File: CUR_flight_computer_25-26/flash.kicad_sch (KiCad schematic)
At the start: 16 parts, among them J1 Micro_SD_Card_Det1, U10 W25Q32JVSS

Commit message: Apply ESDA5V3SC5 MPNs
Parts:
- D11, D12: MPN ESDA6V1SC5 -> ESDA5V3SC5
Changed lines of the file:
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@@
 			)
 		)
-		(property "MPN" "ESDA6V1SC5"
+		(property "MPN" "ESDA5V3SC5"
 			(at 78.74 168.91 0)
 			(effects
@@
 			)
 		)
-		(property "MPN" "ESDA6V1SC5"
+		(property "MPN" "ESDA5V3SC5"
 			(at 107.95 168.91 0)
 			(effects

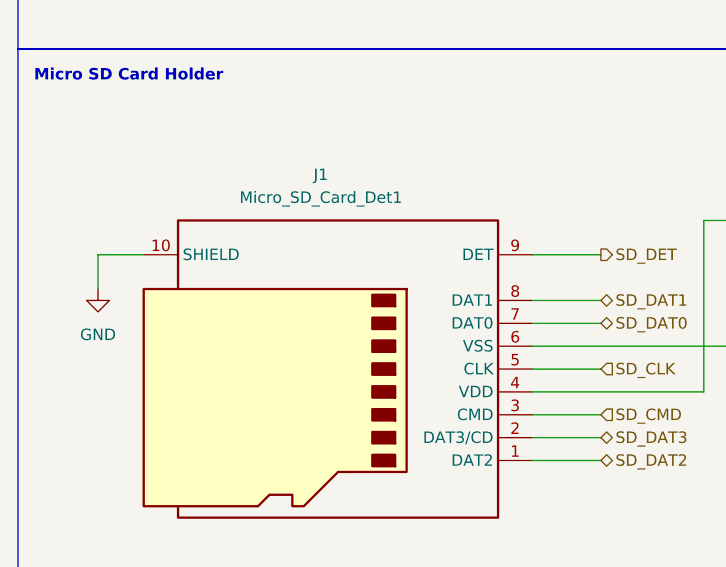
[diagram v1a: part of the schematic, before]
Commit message: BOM optimize 4.7u to 10u caps
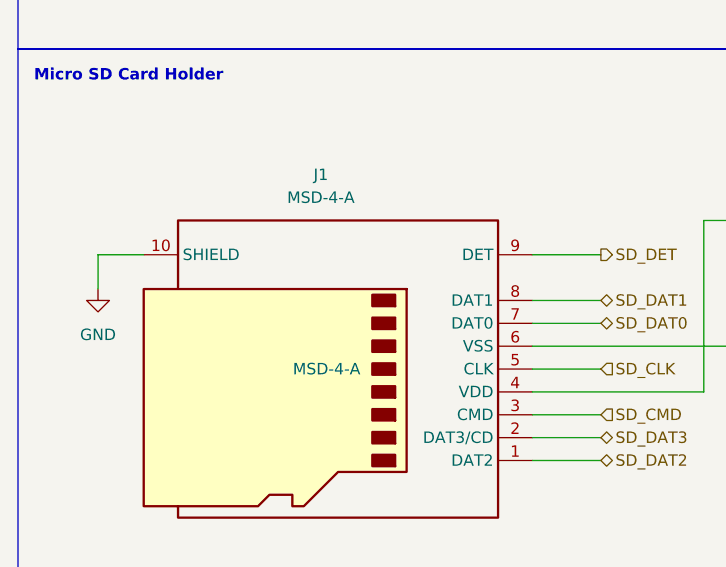
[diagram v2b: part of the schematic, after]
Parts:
- C32: MPN GRM188R61A106ME69D -> LMK107BBJ106MALT
- J1: value Micro_SD_Card_Det1 -> MSD-4-A; MPN (none) -> MSD-4-A
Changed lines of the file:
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@@
 			)
 		)
-		(property "MPN" "GRM188R61A106ME69D"
+		(property "MPN" "LMK107BBJ106MALT"
 			(at 106.68 111.76 0)
 			(effects
@@
 			)
 		)
-		(property "Value" "Micro_SD_Card_Det1"
+		(property "Value" "MSD-4-A"
 			(at 47.625 105.41 0)
 			(effects
@@
 			)
 		)
+		(property "MPN" "MSD-4-A"
+			(at 48.26 124.46 0)
+			(effects
+				(font
+					(size 1.27 1.27)
+				)
+			)
+		)

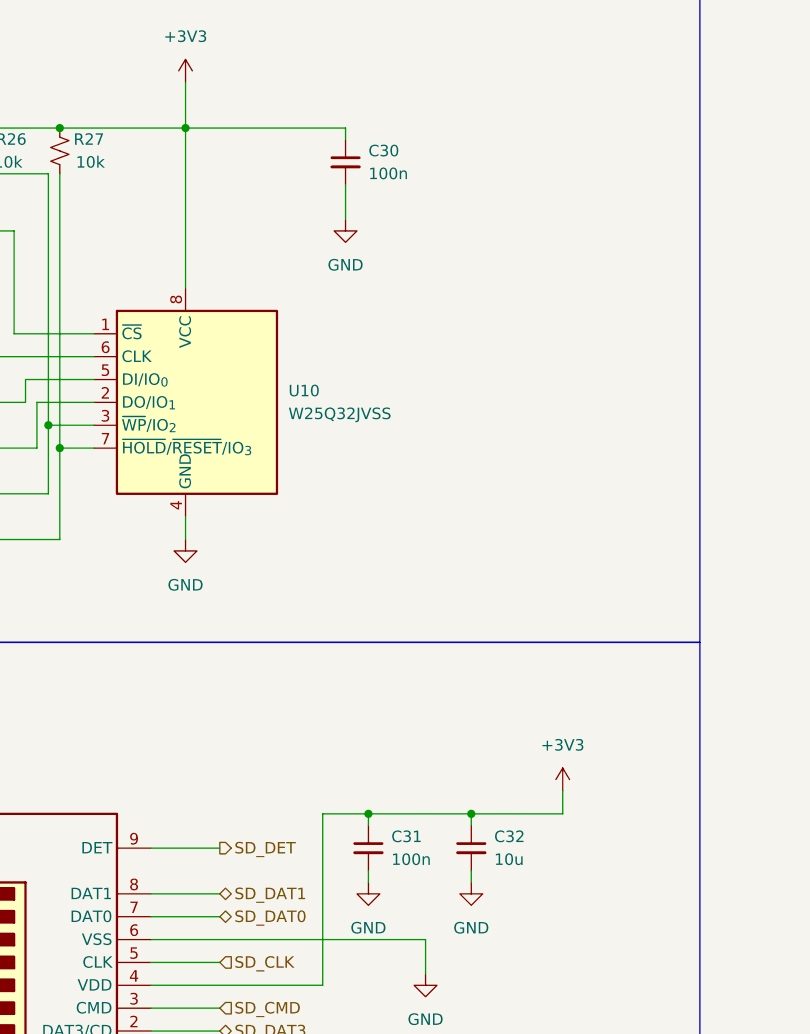
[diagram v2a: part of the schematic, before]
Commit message: BOM optimize 100n to 220n
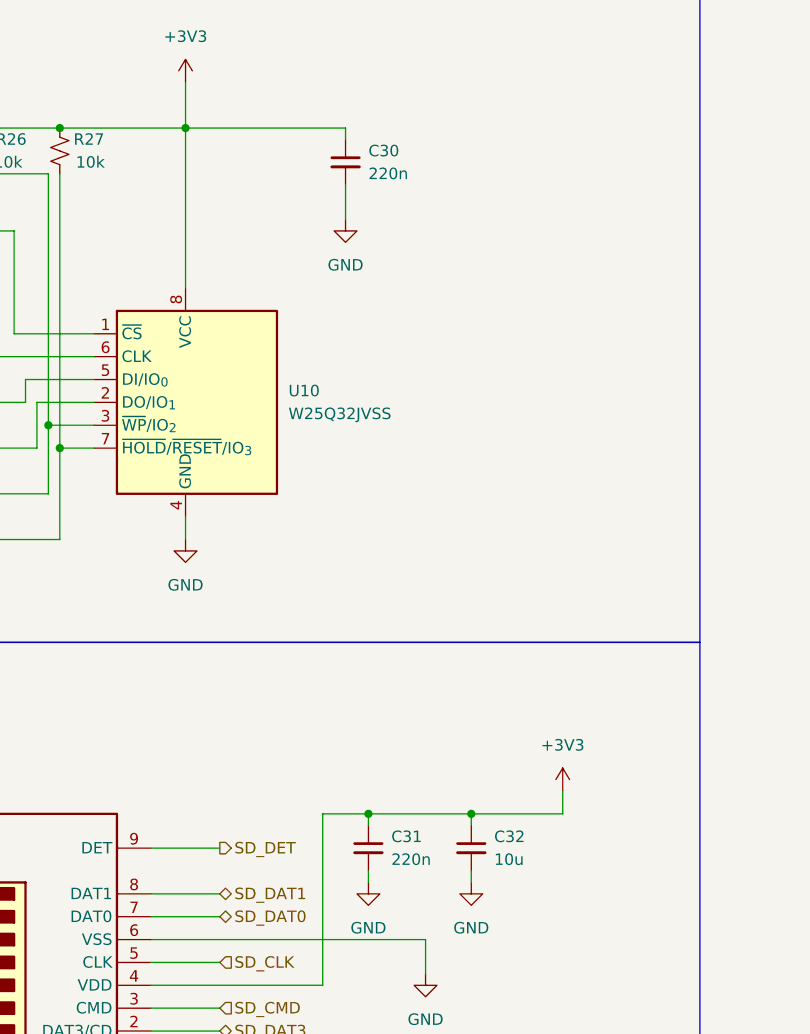
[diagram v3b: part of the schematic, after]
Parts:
- C30, C31: value 100n -> 220n; MPN C0603C104K4RACTU -> 0603B224K250CT
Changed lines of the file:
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@@
 			)
 		)
-		(property "Value" "100n"
+		(property "Value" "220n"
 			(at 95.25 36.8362 0)
 			(effects
@@
 			)
 		)
-		(property "MPN" "C0603C104K4RACTU"
+		(property "MPN" "0603B224K250CT"
 			(at 92.71 35.56 0)
 			(effects
@@
 			)
 		)
-		(property "Value" "100n"
+		(property "Value" "220n"
 			(at 97.79 113.0362 0)
 			(effects
@@
 			)
 		)
-		(property "MPN" "C0603C104K4RACTU"
+		(property "MPN" "0603B224K250CT"
 			(at 95.25 111.76 0)
 			(effects
